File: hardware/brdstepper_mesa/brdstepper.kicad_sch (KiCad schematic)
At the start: 88 parts, among them J2 VM / GND / EN, J3 MOTOR, J4 SMART-SERIAL, J7 SWD, U1 STM32G473CEU6, U2 DRV8876RGTR, U3 DRV8876RGTR, U4 AS5047P-ATSM, U5 TLV75533PDBVR, U6 TPS560430XDBVR, U7 USBLC6-2SC6, U8 SN65HVD30DR, Y1 8MHz

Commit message: brdstepper: split into serial and CAN boards, 0603 passives (WIP, not routed)
- hardware/brdstepper_common: shared parts/board definitions built per
  variant; brdstepper_mesa (A, smart-serial) and brdstepper_can (B, CAN)
  each fit only their own interface parts, MCU pins of the other
  interface left open, HWID divider per variant.
- 0402 resistors and capacitors become 0603; power capacitors stay larger.
- kigen place: GAP_MAX bisects the largest courtyard gap that still
  places every part (0603 on 28 x 28 mm only just fits: gap ~0).
- kigen route: DSN export, BrdRoute, SES import, zone fill (untested end
  to end: first router run still going).

Not done yet: routing on 4 layers, READMEs/BOMs/renders refresh, DEBUGNOTES.

Co-Authored-By: Claude Sonnet 5.5 <noreply@anthropic.com>
Claude-Session: https://claude.ai/code/session_017CSpK2B8oMBAmr39Kq1RSC
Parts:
- removed R7: 10k, Resistor_SMD:R_0402_1005Metric, symbol Device:R
- removed TP4, TP5: TestPoint, TestPoint:TestPoint_THTPad_1.5x1.5mm_Drill0.7mm, symbol Connector:TestPoint
- added J1: USB-C, Connector_USB:USB_C_Receptacle_GCT_USB4105-xx-A_16P_TopMnt_Horizontal, symbol Connector:USB_C_Receptacle_USB2.0_16P
- C10, C11, C12, C13, C14, C15, C16, C17, C18, C19, C20, C22, C23, C25, C26, C27, C29, C30, C31, C32, C33, C34, C36, C37, C38, C4, C5, C8, C9: footprint Capacitor_SMD:C_0402_1005Metric -> Capacitor_SMD:C_0603_1608Metric
- R1, R10, R11, R12, R13, R14, R15, R16, R17, R18, R19, R2, R20, R3, R4, R5, R6, R9: footprint Resistor_SMD:R_0402_1005Metric -> Resistor_SMD:R_0603_1608Metric
- R8: value 10k -> 0; footprint Resistor_SMD:R_0402_1005Metric -> Resistor_SMD:R_0603_1608Metric; Note §6 HWID: A 0 Ω, B 10k -> §6 HWID: variant A, 0 Ω: HWID 0 V
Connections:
- net 5V_USB: now also J1.A4 (VBUS), J1.A9 (VBUS), J1.B4 (VBUS), J1.B9 (VBUS)
- net GND: now also J1.A1 (GND), J1.A12 (GND), J1.B1 (GND), J1.B12 (GND)
- net USB_CC1: now also J1.A5 (CC1)
- net USB_CC2: now also J1.B5 (CC2)
- net USB_DM: now also J1.A7 (D-), J1.B7 (D-)
- net USB_DP: now also J1.A6 (D+), J1.B6 (D+)
- net USB_SHIELD: now also J1.S1 (SHIELD)
- net CAN_STB: no longer names the net of U1.26 (PB13)
- net CAN_TX: no longer names the net of U1.47 (PB9)
- no-connect marks 17 -> 21
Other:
- note added: "USB-C, smart-serial, mounting"
- note added: "brdstepper A: STM32G473 + AS5047P + 2x DRV8876, 28 x 28 mm on the back of a NEMA11 motor. Connections are by net name (net labels): docs/brdstepper_hw.md is the reference. Variant A: U8/J4, smart-serial to a Mesa card."
- note removed: "USB-C, smart-serial (variant A), CAN (variant B), mounting"
- note removed: "brdstepper: STM32G473 + AS5047P + 2x DRV8876, 28 x 28 mm on the back of a NEMA11 motor. Connections are by net name (net labels): docs/brdstepper_hw.md is the reference. Variant A fits U8/J4 (smart-serial to a Mesa card), variant B U9/J5/J6/JP1 (CAN)."
- title: brdstepper: closed-loop NEMA11 stepper drive -> brdstepper: closed-loop NEMA11 stepper drive, smart-serial (Mesa)
- moved on the sheet: C22, H1, H2, H3, H4, J7, R10, R8, R9, TH1, TP1, TP2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

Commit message: brdstepper: USB and SWD as test pads, motor pads on the edge, plane fanout (WIP)
- USB-C connector, its CC/shield parts and ESD chip replaced by four test
  pads (5V, D+, D-, GND) on both boards; SWD header by five test pads.
- Motor pads J3 fixed on the north edge of both boards.
- All fixed parts (the encoder on the shaft axis, holes, edge connectors)
  are locked in the generated board.
- Placement is much looser without the two connectors: serial board
  courtyard gap 0.30 mm.
- kigen route: loads a bare board (pcbnew 7 crashes when tracks are
  removed), GND plane fanout (a via + stub per SMD pad, vias in the MCU's
  exposed pad), In1 hidden from the router, router exit code ignored when
  a session was written.
- DEBUGNOTES: headless pcbnew gotchas.

Needs the BrdRoute plane-net change (not yet committed there); boards are
a routing snapshot, not complete.

Co-Authored-By: Claude Sonnet 5.5 <noreply@anthropic.com>
Claude-Session: https://claude.ai/code/session_017CSpK2B8oMBAmr39Kq1RSC
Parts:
- removed C37: 4.7n, Capacitor_SMD:C_0603_1608Metric, symbol Device:C
- removed J1: USB-C, Connector_USB:USB_C_Receptacle_GCT_USB4105-xx-A_16P_TopMnt_Horizontal, symbol Connector:USB_C_Receptacle_USB2.0_16P
- removed J7: SWD, Connector_PinHeader_1.27mm:PinHeader_1x05_P1.27mm_Vertical_SMD_Pin1Left, symbol Connector_Generic:Conn_01x05
- removed R17, R18: 5.1k, Resistor_SMD:R_0603_1608Metric, symbol Device:R
- removed R19: 1M, Resistor_SMD:R_0603_1608Metric, symbol Device:R
- removed U7: USBLC6-2SC6, Package_TO_SOT_SMD:SOT-23-6, symbol Power_Protection:USBLC6-2SC6
- added TP10: USB D+, TestPoint:TestPoint_Pad_D1.0mm, symbol Connector:TestPoint
- added TP11: USB D-, TestPoint:TestPoint_Pad_D1.0mm, symbol Connector:TestPoint
- added TP12: USB GND, TestPoint:TestPoint_Pad_D1.0mm, symbol Connector:TestPoint
- added TP4: SWD 3V3, TestPoint:TestPoint_Pad_D1.0mm, symbol Connector:TestPoint
- added TP5: SWDIO, TestPoint:TestPoint_Pad_D1.0mm, symbol Connector:TestPoint
- added TP6: NRST, TestPoint:TestPoint_Pad_D1.0mm, symbol Connector:TestPoint
- added TP7: SWCLK, TestPoint:TestPoint_Pad_D1.0mm, symbol Connector:TestPoint
- added TP8: SWD GND, TestPoint:TestPoint_Pad_D1.0mm, symbol Connector:TestPoint
- added TP9: USB 5V, TestPoint:TestPoint_Pad_D1.0mm, symbol Connector:TestPoint
- J3: Note A+ A- B+ B-: solder pads for the motor leads (§4.7 allows p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 -> A+ A- B+ B-: solder pads for the motor leads, on the board 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
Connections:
- net 3V3: now also TP4.1
- net 5V_USB: now also TP9.1
- net GND: now also TP12.1, TP8.1
- net NRST: now also TP6.1
- net SWCLK: now also TP7.1
- net SWDIO: now also TP5.1
- net USB_DM: now also TP11.1
- net USB_DP: now also TP10.1
- no-connect marks 21 -> 19
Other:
- note added: "USB pads, smart-serial, mounting"
- note removed: "USB-C, smart-serial, mounting"
- moved on the sheet: C38, H1, H2, H3, H4, J4, R10, R20, TH1, U8

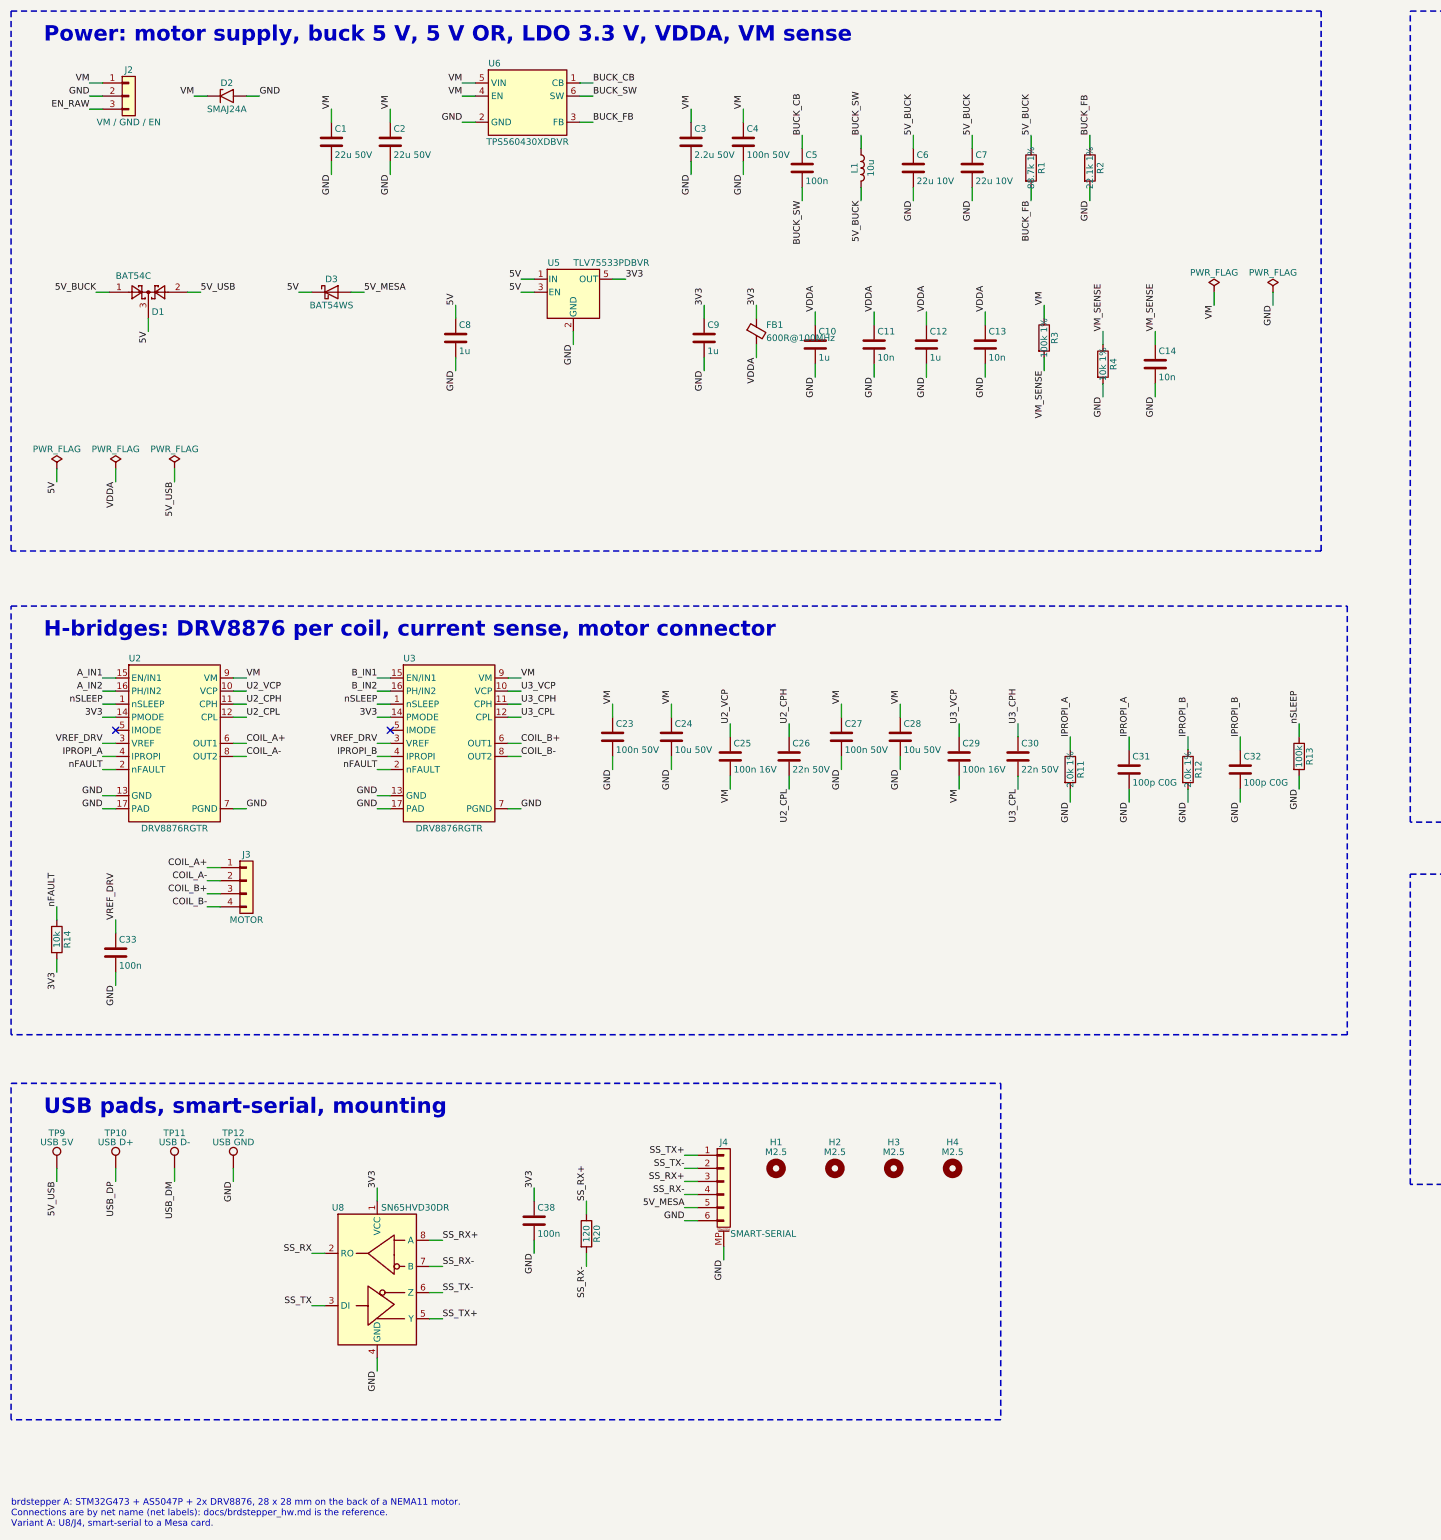
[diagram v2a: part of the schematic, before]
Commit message: brdstepper: drop J2, supply and enable on the signal connectors (WIP)
- Serial board: J4 becomes 8-pin GH (adds VM, EN to TX+/-, RX+/-, 5 V, GND).
- CAN board: J5/J6 become 5-pin GH (adds EN to CANH, CANL, VM, GND).
- No separate supply connector: nothing with supply current beside the
  encoder any more. GH is 1 A per contact (flagged in the BOM notes).

Schematics regenerated; the .kicad_pcb files in this commit are from
before the change and are being re-placed.

Co-Authored-By: Claude Sonnet 5.5 <noreply@anthropic.com>
Claude-Session: https://claude.ai/code/session_017CSpK2B8oMBAmr39Kq1RSC
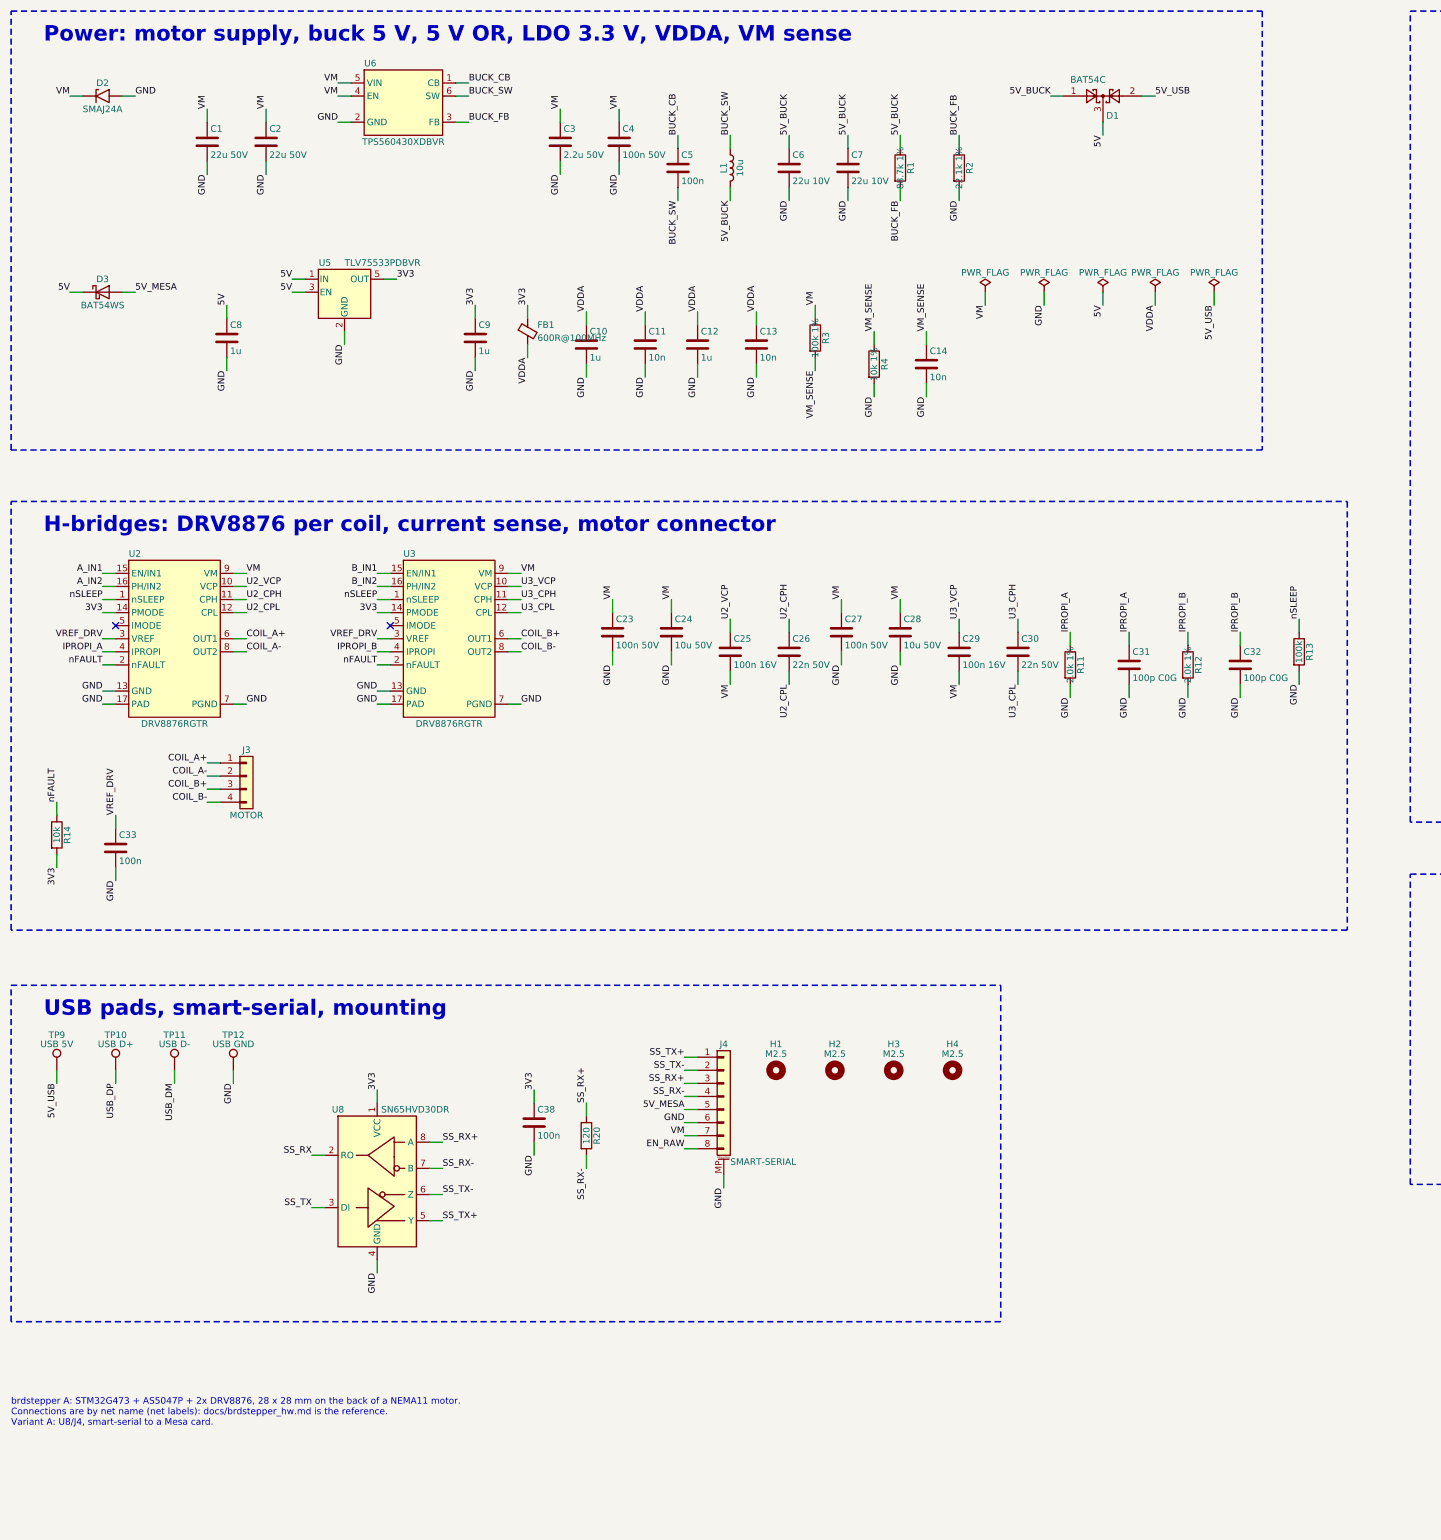
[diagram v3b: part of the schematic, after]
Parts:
- removed J2: VM / GND / EN, Connector_JST:JST_XH_B3B-XH-A_1x03_P2.50mm_Vertical, symbol Connector_Generic:Conn_01x03
- J4: footprint Connector_JST:JST_GH_SM06B-GHS-TB_1x06-1MP_P1.25mm_Horizontal -> Connector_JST:JST_GH_SM08B-GHS-TB_1x08-1MP_P1.25mm_Horizontal; symbol Connector_Generic_MountingPin:Conn_01x06_MountingPin -> Connector_Generic_MountingPin:Conn_01x08_MountingPin; Note variant A; to the Mesa card's RJ45 * -> variant A; to the Mesa card's RJ45 *. Also the motor supply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
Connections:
- net EN_RAW: now also J4.8 (Pin_8)
- net VM: now also J4.7 (Pin_7)
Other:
- moved on the sheet: C1, C10, C11, C12, C13, C14, C2, C23, C24, C25, C26, C27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
